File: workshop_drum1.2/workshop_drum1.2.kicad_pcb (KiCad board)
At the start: 2 copper layers, 50 x 115 mm, 37 parts, among them J1 9v, J2 INPUT, J3 OUTPUT, SW1 POWER, SW2 OSCILLATOR SELECT, SW3 BUTTON, U1 LM358, U2 7414, U3 78L05

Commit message: redid silk - this is the one sent to OSH 5/4/18
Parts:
- LOGO2: footprint zfoot:Logo_S1-2 -> zfoot:S1SMalllllllaf
- LOGO3: footprint zfoot:Logo_OSH-3 -> zfoot:Logo_OSH-4
- moved LOGO2 9.40 mm to (147.9, 54.1)
- moved LOGO4 0.57 mm to (162.3, 83.6)
- moved LOGO3 0.51 mm to (147.9, 45.7)
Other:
- board text added: "&"
- board text added: "THANKS TO"
- board text added: "THE SYNTH LIBRARY OF PORTLAND"

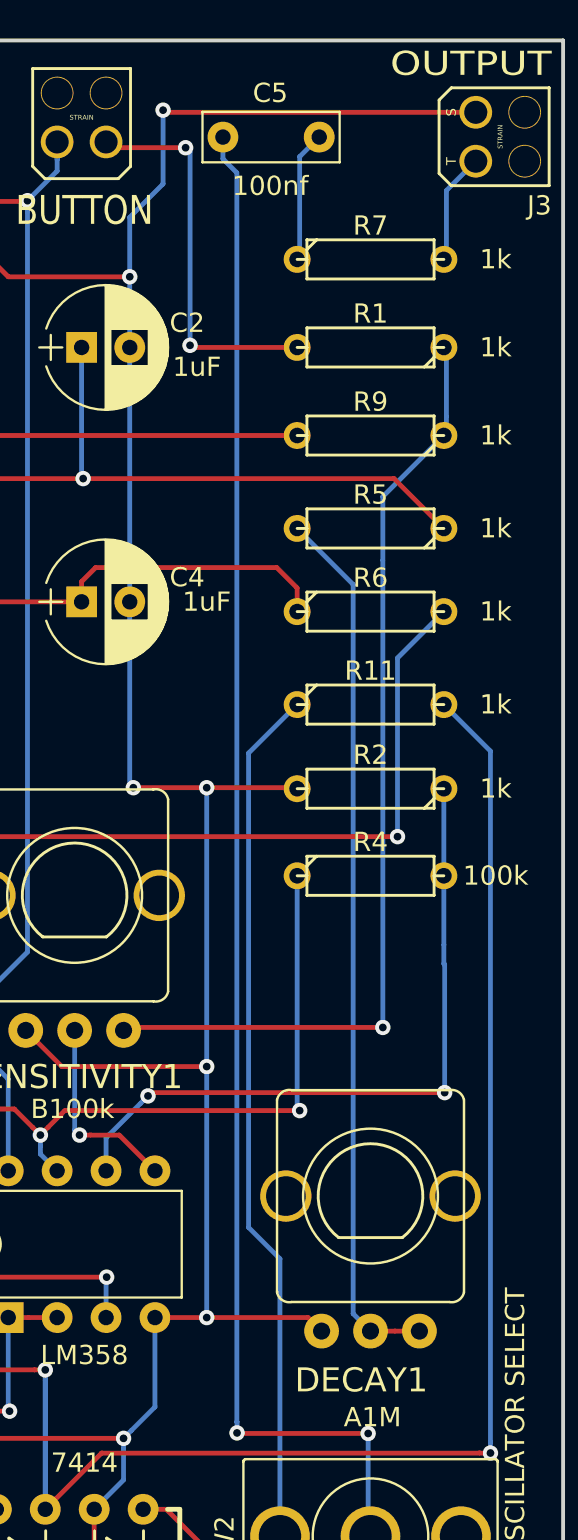
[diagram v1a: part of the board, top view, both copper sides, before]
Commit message: changed C5 from 100nf to 1uF - ceramic to elect cap - generated grbs
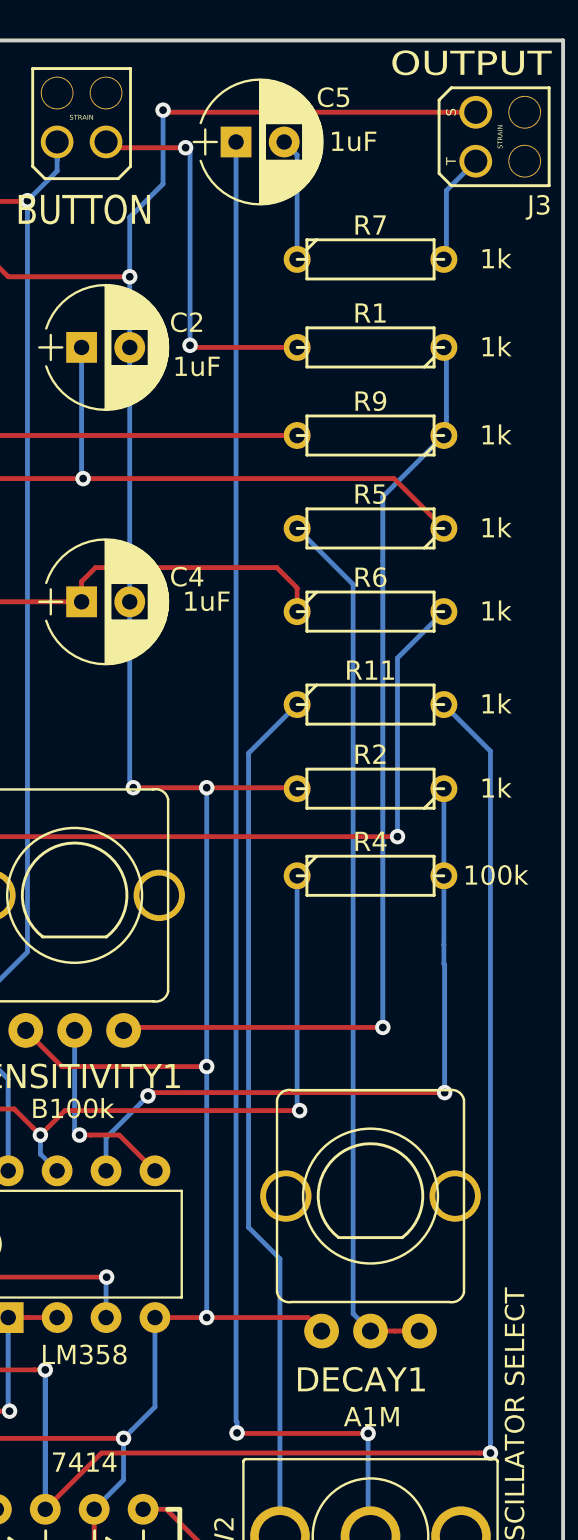
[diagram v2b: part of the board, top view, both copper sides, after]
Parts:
- C5: value 100nf -> 1uF; footprint 4ms-footprints:Cap_Ceramic_TH -> 4ms-footprints:Cap_Electrolytic_TH
- moved C5 4.33 mm to (156.0, 42.7), turned to 0 degrees
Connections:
- R7 pad 1: Net-(C5-Pad1) -> Net-(C5-Pad2)
- SW2 pad 2: Net-(C5-Pad2) -> Net-(C5-Pad1)
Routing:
- net Net-(C5-Pad2): track 79.8 -> 6.37 mm, vias 2 -> 0
- net Net-(C5-Pad1): track 6.77 -> 79.3 mm, vias 0 -> 2
